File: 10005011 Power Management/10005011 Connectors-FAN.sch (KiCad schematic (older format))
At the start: 63 parts, among them IC25 L78M24CDT, IC6 TLV3012AIDBV, J10 BATTERY, J6 FAN, J7 CPU BOARD, J9 TURBINE, T23 IRLML2803, T31 IRLML5103

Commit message: item 10022607
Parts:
- C9: value 0.01uF -> 100nF; footprint 10005011 Power Management:C0603_1 -> 10005011 Power Management:C0402_1; Bom_Footprint 0603 -> (none); Description CAP CER 10000PF 50V X7R 0603 -> CAPACITOR,100NF,16V,+/-10%,X7R,0402; Item Number (none) -> 10022607; Manufacturer (none) -> MURATA; Manufacturer_No (none) -> GRM155R71C104JA88J
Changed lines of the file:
@@
 	13850 7250 13850 7350
-$Comp
-L Device:C C9
-U 1 1 5E9B0C90
-P 13850 7500
-F 0 "C9" H 13965 7591 50  0000 L CNN
-F 1 "0.01uF" H 13965 7500 50  0000 L CNN
-F 2 "10005011 Power Management:C0603_1" H 13888 7350 50  0001 C CNN
-F 3 "https://www.yageo.com/upload/media/product/productsearch/datasheet/mlcc/UPY-GPHC_X7R_6.3V-to-50V_18.pdf" H 13850 7500 50  0001 C CNN
-F 4 "Yageo" H 13850 7500 50  0001 C CNN "Mfgr"
-F 5 "CC0603KRX7R9BB103" H 13850 7500 50  0001 C CNN "Mfgr_PN"
-F 6 "Digi-Key" H 13850 7500 50  0001 C CNN "Source"
-F 7 "311-1085-1-ND" H 13850 7500 50  0001 C CNN "Source_PN"
-F 8 "0603" H 13965 7409 50  0000 L CNN "Bom_Footprint"
-F 9 "CAP CER 10000PF 50V X7R 0603" H 13850 7500 50  0001 C CNN "Description"
-F 10 "X7R" H 13850 7500 50  0001 C CNN "Dielectric"
-F 11 "50V" H 13850 7500 50  0001 C CNN "Voltage"
-	1    13850 7500
-	1    0    0    -1
-$EndComp
 $Comp
 L 10005011_Power_Management:BAT54 D20
@@
 	1    0    0    -1
 $EndComp
+$Comp
+L Device:C C9
+U 1 1 5E9B0C90
+P 13850 7500
+F 0 "C9" H 13965 7546 50  0000 L CNN
+F 1 "100nF" H 13965 7455 50  0000 L CNN
+F 2 "10005011 Power Management:C0402_1" H 13888 7350 50  0001 C CNN
+F 3 "https://www.yageo.com/upload/media/product/productsearch/datasheet/mlcc/UPY-GPHC_X7R_6.3V-to-50V_18.pdf" H 13850 7500 50  0001 C CNN
+F 4 "Yageo" H 13850 7500 50  0001 C CNN "Mfgr"
+F 5 "CC0603KRX7R9BB103" H 13850 7500 50  0001 C CNN "Mfgr_PN"
+F 6 "Digi-Key" H 13850 7500 50  0001 C CNN "Source"
+F 7 "311-1085-1-ND" H 13850 7500 50  0001 C CNN "Source_PN"
+F 8 "CAPACITOR,100NF,16V,+/-10%,X7R,0402" H 13850 7500 50  0001 C CNN "Description"
+F 9 "X7R" H 13850 7500 50  0001 C CNN "Dielectric"
+F 10 "50V" H 13850 7500 50  0001 C CNN "Voltage"
+F 11 "10022607" H 13850 7500 50  0001 C CNN "Item Number"
+F 12 "MURATA" H 13850 7500 50  0001 C CNN "Manufacturer"
+F 13 "GRM155R71C104JA88J" H 13850 7500 50  0001 C CNN "Manufacturer_No"
+	1    13850 7500
+	1    0    0    -1
+$EndComp

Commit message: update PCB deleting double lines in the edge layer to create a board outline and update the USB_A footprints and IC11
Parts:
- R114: footprint 10005011 Power Management:R0603_1 -> 10005011 Power Management:RC1206_1; Bom_Footprint 0603 -> (none); Description RES SMD 1.5K OHM 1% 1/10W 0603 -> RESISTOR,1.5K OHM,0.250W,+/-1%,1206; Item Number (none) -> 10022740; Mfgr Panasonic Electronic Components -> YAGEO_RMS1; Mfgr_PN ERJ-3EKF1501V -> RC1206FR-071K5L; Source Digi-Key -> (none); Source_PN P1.50KHCT-ND -> (none); Tolerance 1% -> (none); Wattage 1/10W -> (none)
- R115: footprint 10005011 Power Management:R0603_1 -> 10005011 Power Management:RC1206_1; Bom_Footprint 0603 -> (none); Description RES SMD 1K OHM 1% 1/10W 0603 -> RESISTOR,1 KOHM,0.25W,+/-1%,1206; Item Number (none) -> 10022557; Mfgr Bourns Inc. -> YAGEO_RMS1; Mfgr_PN CR0603-FX-1001ELF -> RC1206FR-071KL; Source Digi-Key -> (none); Source_PN CR0603-FX-1001ELFCT-ND -> (none); Tolerance 1% -> (none); Wattage 1/10W -> (none)
- R116: footprint 10005011 Power Management:R0603_1 -> 10005011 Power Management:RC1206_1; Bom_Footprint 0603 -> (none); Description RES SMD 100 OHM 1% 1/10W 0603 -> RESISTOR,100 OHM,0.25W,+/-1%,1206; Item Number (none) -> 10022742; Manufacturer (none) -> YAGEO/PHYCOMP_RMS1; Manufacturer No (none) -> 232272461001L; Mfgr Bourns Inc. -> (none); Mfgr_PN CR0603-FX-1000ELF -> (none); Source Digi-Key -> (none); Source_PN CR0603-FX-1000ELFCT-ND -> (none); Tolerance 1% -> (none); Wattage 1/10W -> (none)
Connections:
- net +24VUTIL: now also C110.2; no longer C110.1
- net PGND: now also C110.1; no longer C110.2
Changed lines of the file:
@@
 Wire Wire Line
 	12950 8450 12950 8650
-Text Notes 3700 1050 0    50   ~ 0
-ideally, a couple of the pins might be bypassed to PGND instead of GND,\nbut it doesn't really matter because the CPU board combines the grounds.
 Connection ~ 5050 1650
 Wire Wire Line
@@
 	1    0    0    -1
 $EndComp
-$Comp
-L Device:Jumper_NC_Small JPL3
-U 1 1 5EB10713
-P 4200 7600
-F 0 "JPL3" V 4154 7552 50  0000 R CNN
-F 1 "LINK" V 4245 7552 50  0000 R CNN
-F 2 "10005011 Power Management:GDCAFE-F_FERME_1" H 4200 7600 50  0001 C CNN
-F 3 "~" H 4200 7600 50  0001 C CNN
-	1    4200 7600
-	0    1    1    0
-$EndComp
 Wire Wire Line
 	4200 7450 4200 7300
@@
 U 1 1 5F497A72
 P 3750 9850
-F 0 "C110" H 3865 9896 50  0000 L CNN
-F 1 "100nF" H 3865 9805 50  0000 L CNN
+F 0 "C110" H 3865 9804 50  0000 L CNN
+F 1 "100nF" H 3865 9895 50  0000 L CNN
 F 2 "10005011 Power Management:C0805_1" H 3788 9700 50  0001 C CNN
 F 3 "https://www.yageo.com/upload/media/product/productsearch/datasheet/mlcc/UPY-GPHC_X7R_6.3V-to-50V_18.pdf" H 3750 9850 50  0001 C CNN
@@
 F 11 "10022135" H 3750 9850 50  0001 C CNN "Item Number"
 	1    3750 9850
-	1    0    0    -1
+	1    0    0    1
 $EndComp
 $Comp
@@
 $EndComp
 $Comp
-L Device:R R115
-U 1 1 5E962213
-P 9650 7300
-F 0 "R115" H 9581 7391 50  0000 R CNN
-F 1 "1k" H 9581 7300 50  0000 R CNN
-F 2 "10005011 Power Management:R0603_1" V 9580 7300 50  0001 C CNN
-F 3 "https://www.bourns.com/docs/Product-Datasheets/CHPREZTR.pdf" H 9650 7300 50  0001 C CNN
-F 4 "Bourns Inc." H 9650 7300 50  0001 C CNN "Mfgr"
-F 5 "CR0603-FX-1001ELF" H 9650 7300 50  0001 C CNN "Mfgr_PN"
-F 6 "Digi-Key" H 9650 7300 50  0001 C CNN "Source"
-F 7 "CR0603-FX-1001ELFCT-ND" H 9650 7300 50  0001 C CNN "Source_PN"
-F 8 "0603" H 9581 7209 50  0000 R CNN "Bom_Footprint"
-F 9 "RES SMD 1K OHM 1% 1/10W 0603" H 9650 7300 50  0001 C CNN "Description"
-F 10 "1%" H 9650 7300 50  0001 C CNN "Tolerance"
-F 11 "1/10W" H 9650 7300 50  0001 C CNN "Wattage"
-	1    9650 7300
-	1    0    0    -1
-$EndComp
-$Comp
 L Device:R R114
 U 1 1 5E962F48
@@
 F 0 "R114" H 9720 7891 50  0000 L CNN
 F 1 "1.5k" H 9720 7800 50  0000 L CNN
-F 2 "10005011 Power Management:R0603_1" V 9580 7800 50  0001 C CNN
+F 2 "10005011 Power Management:RC1206_1" V 9580 7800 50  0001 C CNN
 F 3 "https://industrial.panasonic.com/cdbs/www-data/pdf/RDA0000/AOA0000C304.pdf" H 9650 7800 50  0001 C CNN
-F 4 "Panasonic Electronic Components" H 9650 7800 50  0001 C CNN "Mfgr"
-F 5 "ERJ-3EKF1501V" H 9650 7800 50  0001 C CNN "Mfgr_PN"
-F 6 "Digi-Key" H 9650 7800 50  0001 C CNN "Source"
-F 7 "P1.50KHCT-ND" H 9650 7800 50  0001 C CNN "Source_PN"
-F 8 "0603" H 9720 7709 50  0000 L CNN "Bom_Footprint"
-F 9 "RES SMD 1.5K OHM 1% 1/10W 0603" H 9650 7800 50  0001 C CNN "Description"
-F 10 "1%" H 9650 7800 50  0001 C CNN "Tolerance"
-F 11 "1/10W" H 9650 7800 50  0001 C CNN "Wattage"
+F 4 "YAGEO_RMS1" H 9650 7800 50  0001 C CNN "Mfgr"
+F 5 "RC1206FR-071K5L" H 9650 7800 50  0001 C CNN "Mfgr_PN"
+F 6 "RESISTOR,1.5K OHM,0.250W,+/-1%,1206" H 9650 7800 50  0001 C CNN "Description"
+F 7 "10022740" H 9650 7800 50  0001 C CNN "Item Number"
 	1    9650 7800
 	1    0    0    -1
@@
 F 0 "R116" H 11420 8491 50  0000 L CNN
 F 1 "100" H 11420 8400 50  0000 L CNN
-F 2 "10005011 Power Management:R0603_1" V 11280 8400 50  0001 C CNN
+F 2 "10005011 Power Management:RC1206_1" V 11280 8400 50  0001 C CNN
 F 3 "https://www.bourns.com/docs/Product-Datasheets/CHPREZTR.pdf" H 11350 8400 50  0001 C CNN
-F 4 "Bourns Inc." H 11350 8400 50  0001 C CNN "Mfgr"
-F 5 "CR0603-FX-1000ELF" H 11350 8400 50  0001 C CNN "Mfgr_PN"
-F 6 "Digi-Key" H 11350 8400 50  0001 C CNN "Source"
-F 7 "CR0603-FX-1000ELFCT-ND" H 11350 8400 50  0001 C CNN "Source_PN"
-F 8 "0603" H 11420 8309 50  0000 L CNN "Bom_Footprint"
-F 9 "RES SMD 100 OHM 1% 1/10W 0603" H 11350 8400 50  0001 C CNN "Description"
-F 10 "1%" H 11350 8400 50  0001 C CNN "Tolerance"
-F 11 "1/10W" H 11350 8400 50  0001 C CNN "Wattage"
+F 4 "RESISTOR,100 OHM,0.25W,+/-1%,1206" H 11350 8400 50  0001 C CNN "Description"
+F 5 "10022742" H 11350 8400 50  0001 C CNN "Item Number"
+F 6 "YAGEO/PHYCOMP_RMS1" H 11350 8400 50  0001 C CNN "Manufacturer"
+F 7 "232272461001L" H 11350 8400 50  0001 C CNN "Manufacturer No"
 	1    11350 8400
 	1    0    0    -1
@@
 	1    0    0    -1
 $EndComp
+$Comp
+L Device:R R115
+U 1 1 5E962213
+P 9650 7300
+F 0 "R115" H 9581 7391 50  0000 R CNN
+F 1 "1k" H 9581 7300 50  0000 R CNN
+F 2 "10005011 Power Management:RC1206_1" V 9580 7300 50  0001 C CNN
+F 3 "https://www.bourns.com/docs/Product-Datasheets/CHPREZTR.pdf" H 9650 7300 50  0001 C CNN
+F 4 "YAGEO_RMS1" H 9650 7300 50  0001 C CNN "Mfgr"
+F 5 "RC1206FR-071KL" H 9650 7300 50  0001 C CNN "Mfgr_PN"
+F 6 "RESISTOR,1 KOHM,0.25W,+/-1%,1206" H 9650 7300 50  0001 C CNN "Description"
+F 7 "10022557" H 9650 7300 50  0001 C CNN "Item Number"
+	1    9650 7300
+	1    0    0    -1
+$EndComp
+$Comp
+L Device:Jumper_NC_Small JPL3
+U 1 1 5EB10713
+P 4200 7600
+F 0 "JPL3" V 4154 7552 50  0000 R CNN
+F 1 "LINK" V 4245 7552 50  0000 R CNN
+F 2 "10005011 Power Management:GDCAFE-F_FERME_1" H 4200 7600 50  0001 C CNN
+F 3 "~" H 4200 7600 50  0001 C CNN
+	1    4200 7600
+	0    1    1    0
+$EndComp
+Text Notes 3700 1050 0    50   ~ 0
+ideally, a couple of the pins might be bypassed to PGND instead of GND,\nbut it doesn't really matter because the CPU board combines the grounds.
 $EndSCHEMATC

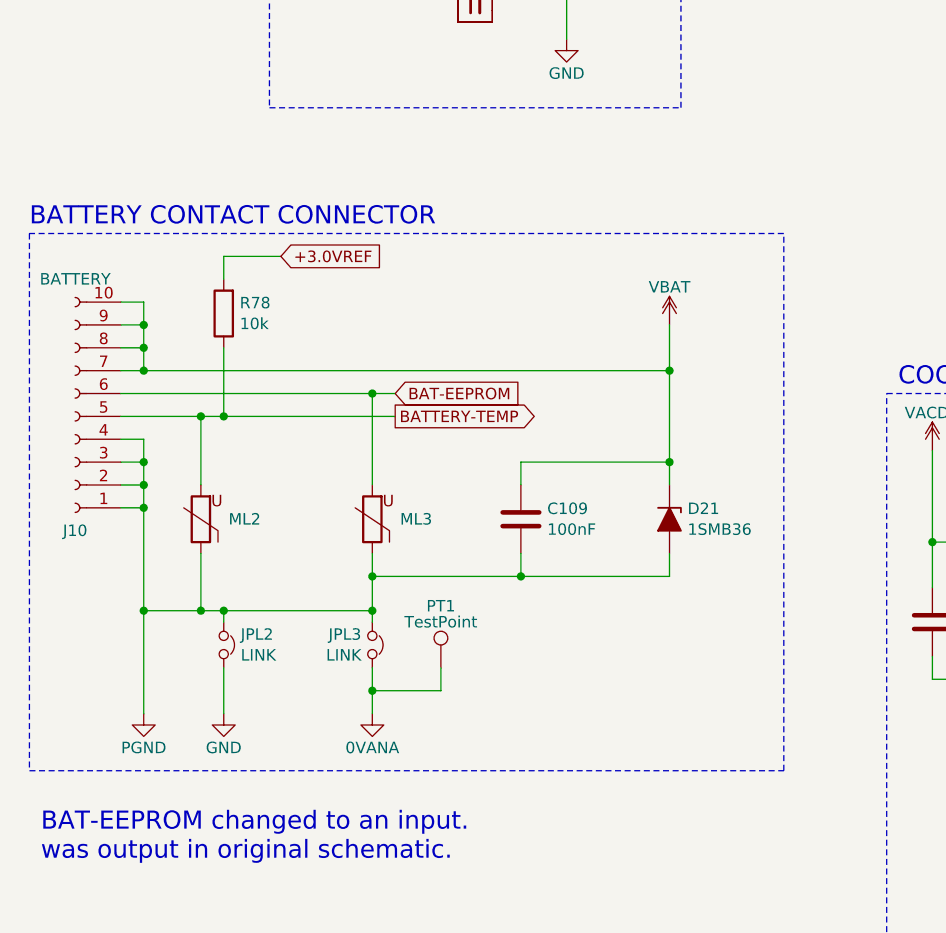
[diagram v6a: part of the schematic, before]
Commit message: change CR1-BIS to ZCR1 so that kicad does not think it is missing annotation, do the same in the PCB to be able to read netlist without components getting erased and placed new
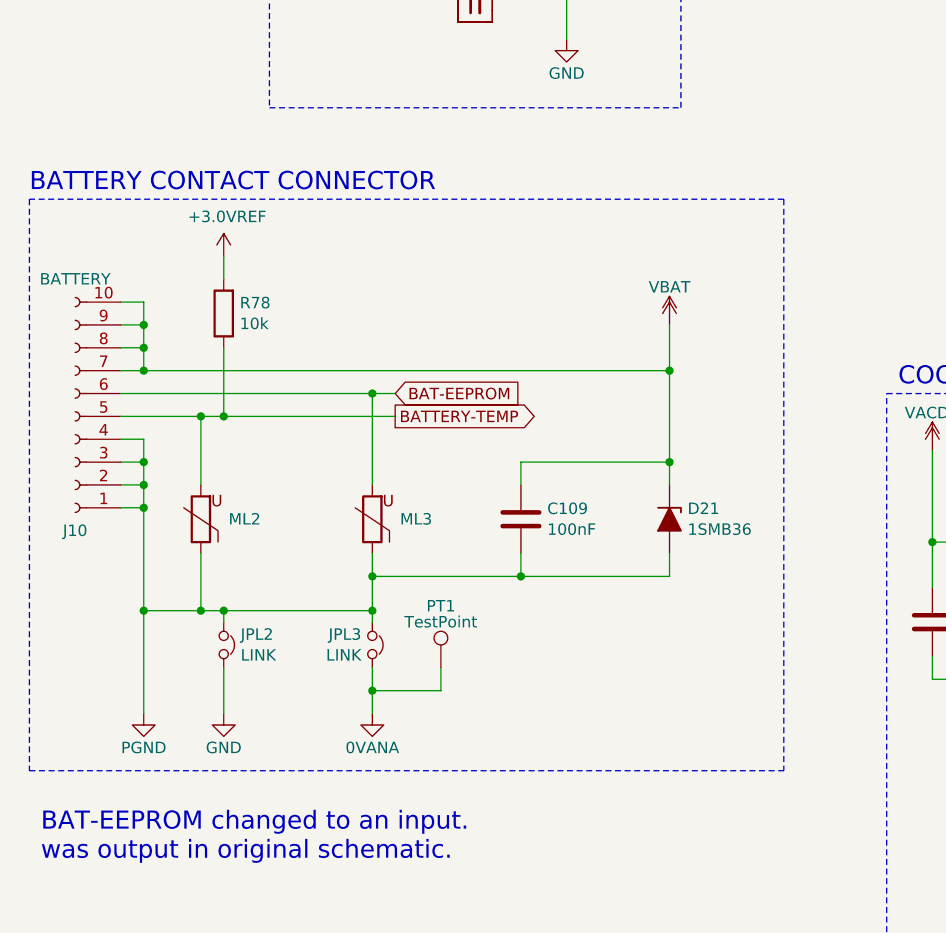
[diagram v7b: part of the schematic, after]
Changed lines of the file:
@@
 Wire Wire Line
 	3550 6600 4300 6600
-Wire Wire Line
-	3550 5900 3800 5900
-Wire Notes Line
-	2700 5800 2700 8150
 Wire Notes Line
 	2700 8150 6000 8150
 Wire Notes Line
-	6000 8150 6000 5800
-Wire Notes Line
-	6000 5800 2700 5800
-Text Notes 2700 5775 0    79   ~ 0
+	6000 5650 2700 5650
+Text Notes 2700 5625 0    79   ~ 0
 BATTERY CONTACT CONNECTOR
 $Comp
@@
 Text GLabel 14450 8050 2    50   Output ~ 0
 FAN-SPEED
-Text GLabel 3800 5900 2    50   Input ~ 0
-+3.0VREF
 Text GLabel 4300 6500 2    50   Input ~ 0
 BAT-EEPROM
@@
 Text Notes 3700 1050 0    50   ~ 0
 ideally, a couple of the pins might be bypassed to PGND instead of GND,\nbut it doesn't really matter because the CPU board combines the grounds.
+$Comp
+L 10005011_Power_Management:+3.0VREF #PWR0286
+U 1 1 5EA1946D
+P 3550 5900
+F 0 "#PWR0286" H 3550 5750 50  0001 C CNN
+F 1 "+3.0VREF" H 3565 6073 50  0000 C CNN
+F 2 "" H 3550 5900 50  0001 C CNN
+F 3 "" H 3550 5900 50  0001 C CNN
+	1    3550 5900
+	1    0    0    -1
+$EndComp
+Wire Notes Line
+	6000 5650 6000 8150
+Wire Notes Line
+	2700 5650 2700 8150
 $EndSCHEMATC

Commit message: rename DPAK
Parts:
- IC25: footprint 10005011 Power Management:DPAK_1 -> 10005011 Power Management:DPAK_1b
